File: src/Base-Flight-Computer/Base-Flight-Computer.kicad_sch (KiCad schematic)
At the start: 50 parts, among them J1 Jumper_NO, P1 1984659, P2 USB, P3 0530470610, P4 1546551-2, Q1 QS5U17TR, Q2 2N7002W-7-F, Q3 2N7002W-7-F, Q4 QS5U17TR, U1 STM32G4A1KEU6, U2 BMP390, U3 LMS8117AMP-3.3_NOPB, Y1 ECS-240-18-33-JGN-TR

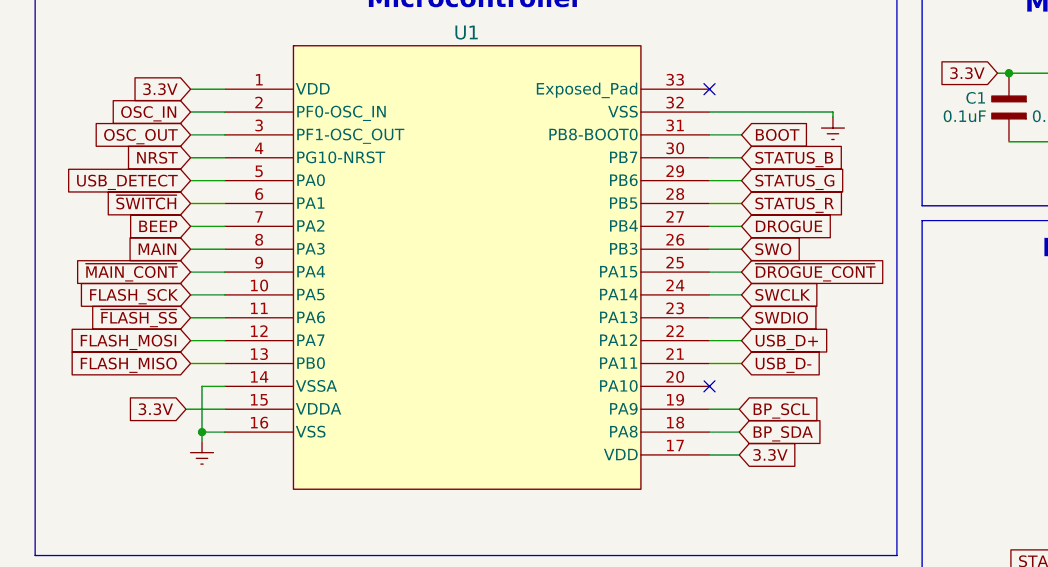
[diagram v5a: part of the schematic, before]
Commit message: added battery measurement circuit
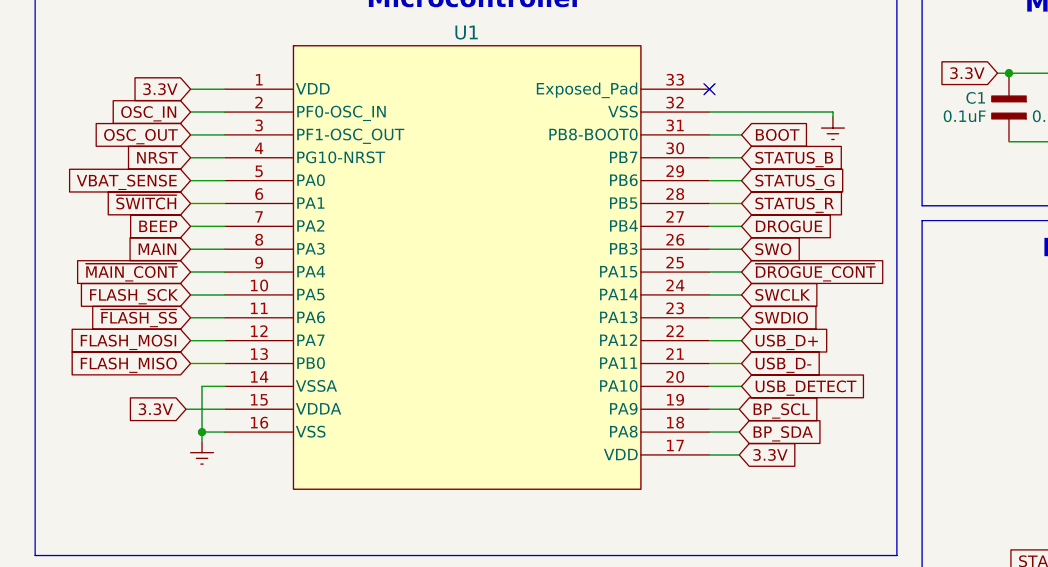
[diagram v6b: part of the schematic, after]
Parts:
- D1: footprint LED_CLMVC-FKA-CL1D1L71BB7C3C3 -> (none)
- D2, D4: footprint SOD-123FL_MCC -> (none)
- U1: footprint QFPN_4A1KEU6_STM -> (none)
- U2: footprint XDCR_BMP390L -> (none)
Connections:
- net USB_DETECT: now also U1.20 (PA10); no longer U1.5 (PA0)
- new net VBAT_SENSE: U1.5 (PA0)
- no-connect marks 4 -> 3
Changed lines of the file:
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@@
   (junction (at 45.466 167.894) (diameter 0) (color 0 0 0 0)
   )
-  (no_connect (at 90.932 65.532))
   (no_connect (at 75.184 123.444))
   (no_connect (at 132.207 116.84))
@@
     (stroke (width 0) (type default))
   )
+  (wire (pts (xy 90.932 65.532) (xy 94.488 65.532))
+    (stroke (width 0) (type default))
+  )
   (wire (pts (xy 218.694 72.39) (xy 218.694 73.152))
     (stroke (width 0) (type default))
@@
     (stroke (width 0) (type default))
   )
+  (wire (pts (xy 33.274 42.672) (xy 37.084 42.672))
+    (stroke (width 0) (type default))
+  )
   (wire (pts (xy 150.368 109.22) (xy 152.146 109.22))
     (stroke (width 0) (type default))
@@
   )
   (wire (pts (xy 245.872 140.97) (xy 249.047 140.97))
-    (stroke (width 0) (type default))
-  )
-  (wire (pts (xy 33.274 42.672) (xy 37.084 42.672))
     (stroke (width 0) (type default))
   )
@@
     )
   )
+  (global_label "VBAT_SENSE" (shape input) (at 33.274 42.672 180) (fields_autoplaced)
+    (effects (font (size 1.27 1.27)) (justify right))
+    (property "Intersheetrefs" "${INTERSHEET_REFS}" (at 18.9383 42.672 0)
+      (effects (font (size 1.27 1.27)) (justify right) hide)
+    )
+  )
   (global_label "STATUS_R" (shape input) (at 135.509 90.043 180) (fields_autoplaced)
     (effects (font (size 1.27 1.27)) (justify right))
@@
     )
   )
-  (global_label "USB_DETECT" (shape input) (at 33.274 42.672 180) (fields_autoplaced)
-    (effects (font (size 1.27 1.27)) (justify right))
-    (property "Intersheetrefs" "${INTERSHEET_REFS}" (at 19.3099 42.5926 0)
-      (effects (font (size 1.27 1.27)) (justify right) hide)
+  (global_label "USB_DETECT" (shape input) (at 94.488 65.532 0) (fields_autoplaced)
+    (effects (font (size 1.27 1.27)) (justify left))
+    (property "Intersheetrefs" "${INTERSHEET_REFS}" (at 108.4521 65.4526 0)
+      (effects (font (size 1.27 1.27)) (justify left) hide)
     )
   )
@@
       (effects (font (size 1.27 1.27)))
     )
-    (property "Footprint" "XDCR_BMP390L" (at 52.324 138.049 0)
+    (property "Footprint" "" (at 52.324 138.049 0)
       (effects (font (size 1.27 1.27)) (justify left bottom) hide)
     )
@@
       (effects (font (size 1.524 1.524)) hide)
     )
-    (property "Footprint" "SOD-123FL_MCC" (at 39.878 175.514 0)
+    (property "Footprint" "" (at 39.878 175.514 0)
       (effects (font (size 1.524 1.524)) hide)
     )
@@
       (effects (font (size 1.524 1.524)) hide)
     )
-    (property "Footprint" "QFPN_4A1KEU6_STM" (at 36.957 32.512 0)
+    (property "Footprint" "" (at 36.957 32.512 0)
       (effects (font (size 1.27 1.27) italic) hide)
     )
@@
       (effects (font (size 1.524 1.524)) hide)
     )
-    (property "Footprint" "SOD-123FL_MCC" (at 39.878 189.992 0)
+    (property "Footprint" "" (at 39.878 189.992 0)
       (effects (font (size 1.524 1.524)) hide)
     )
@@
       (effects (font (size 1.27 1.27)) (justify left bottom) hide)
     )
-    (property "Footprint" "LED_CLMVC-FKA-CL1D1L71BB7C3C3" (at 138.684 76.708 0)
-      (effects (font (size 1.27 1.27)) (justify left bottom) hide)
-    )
+    (property "Footprint" "" (at 138.684 76.708 0)
+      (effects (font (size 1.27 1.27)) (justify left bottom) hide)
+    )

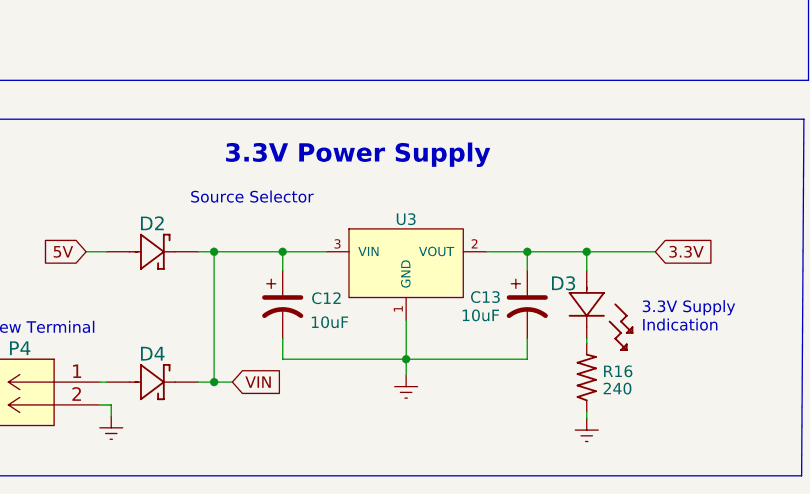
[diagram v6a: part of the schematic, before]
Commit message: swapped out linear regulator for reduced form factor
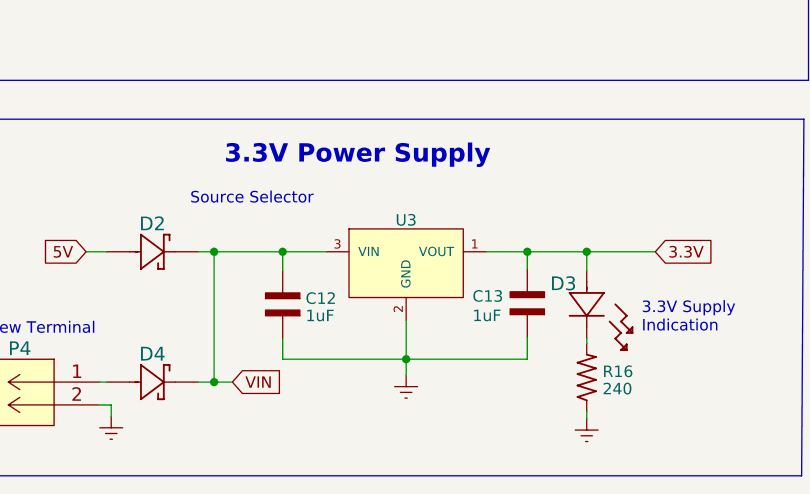
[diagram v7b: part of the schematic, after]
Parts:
- removed C12, C13: 10uF, Flight-Computer-Lite:T491A106K010AT, symbol Flight-Computer:CAP_Polar
- removed U3: LMS8117AMP-3.3_NOPB, Flight-Computer-Lite:LMS8117AMP-3.3NOPB, symbol Flight-Computer:LMS8117AMP-3.3_NOPB
- added C12, C13: 1uF, Base-Flight-Computer:CAP_0603, symbol Base-Flight-Computer:CAP_0603
- added U3: LMS8117AMP-3.3_NOPB, Base-Flight-Computer:AP7370-33Y-13, symbol Base-Flight-Computer:AP7370-33Y-13
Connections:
- net 3.3V: now also C13.1, U3.1 (VOUT)
- net Earth: now also C12.2, C13.2, U3.2 (GND)
- net VIN: now also C12.1, U3.3 (VIN)

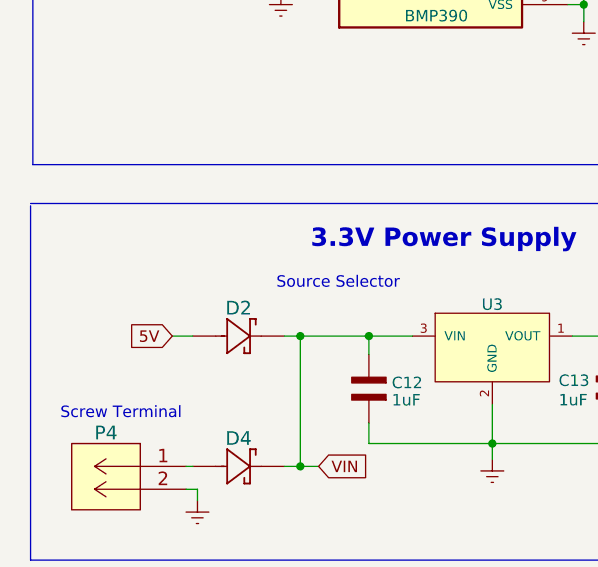
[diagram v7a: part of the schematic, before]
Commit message: removed extra units from JST connector symbol
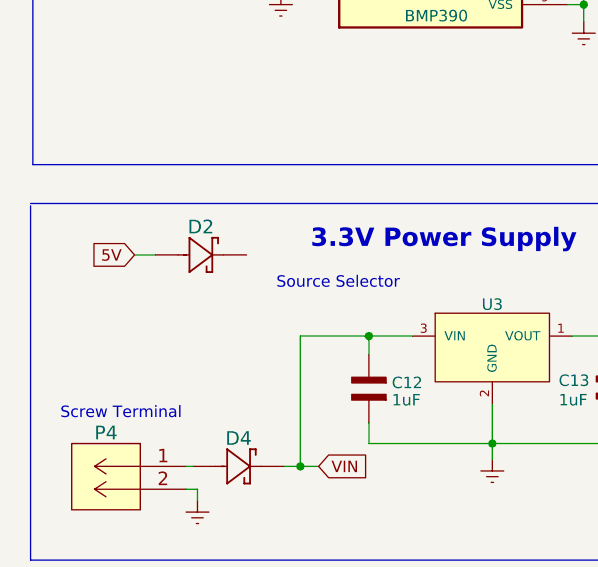
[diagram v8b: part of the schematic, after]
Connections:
- net VIN: no longer D2.1
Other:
- moved on the sheet: D2
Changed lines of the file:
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@@
   (junction (at 237.998 61.722) (diameter 0) (color 0 0 0 0)
-  )
-  (junction (at 45.466 167.894) (diameter 0) (color 0 0 0 0)
   )
   (no_connect (at 75.184 123.444))
@@
     (stroke (width 0) (type default))
   )
-  (wire (pts (xy 43.688 167.894) (xy 45.466 167.894))
-    (stroke (width 0) (type default))
-  )
   (wire (pts (xy 146.431 144.272) (xy 148.336 144.272))
     (stroke (width 0) (type default))
@@
     (stroke (width 0) (type default))
   )
-  (wire (pts (xy 31.242 167.894) (xy 33.528 167.894))
+  (wire (pts (xy 27.051 158.877) (xy 29.337 158.877))
     (stroke (width 0) (type default))
   )
@@
     )
   )
-  (global_label "5V" (shape input) (at 31.242 167.894 180) (fields_autoplaced)
-    (effects (font (size 1.27 1.27)) (justify right))
-    (property "Intersheetrefs" "${INTERSHEET_REFS}" (at 26.6197 167.8146 0)
+  (global_label "5V" (shape input) (at 27.051 158.877 180) (fields_autoplaced)
+    (effects (font (size 1.27 1.27)) (justify right))
+    (property "Intersheetrefs" "${INTERSHEET_REFS}" (at 22.4287 158.7976 0)
       (effects (font (size 1.27 1.27)) (justify right) hide)
     )
@@
     )
   )
-  (symbol (lib_id "Flight-Computer:SM5819PL-TP") (at 38.608 167.894 0) (unit 1)
+  (symbol (lib_id "Flight-Computer:SM5819PL-TP") (at 34.417 158.877 0) (unit 1)
     (in_bom yes) (on_board yes) (dnp no) (fields_autoplaced)
-    (property "Reference" "D2" (at 38.608 164.7967 0)
+    (property "Reference" "D2" (at 34.417 155.7797 0)
       (effects (font (size 1.524 1.524)))
     )
-    (property "Value" "SM5819PL-TP" (at 39.878 172.974 0)
+    (property "Value" "SM5819PL-TP" (at 35.687 163.957 0)
       (effects (font (size 1.524 1.524)) hide)
     )
-    (property "Footprint" "" (at 39.878 175.514 0)
+    (property "Footprint" "" (at 35.687 166.497 0)
       (effects (font (size 1.524 1.524)) hide)
     )
-    (property "Datasheet" "" (at 33.528 167.894 0)
+    (property "Datasheet" "" (at 29.337 158.877 0)
       (effects (font (size 1.524 1.524)) hide)
     )
